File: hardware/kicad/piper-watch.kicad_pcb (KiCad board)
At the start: 2 copper layers, 70 x 50 mm, 15 parts, among them J1 19V in (switched, fused), J3 motor: A1 A2 B1 B2, J4 to ESP32: STEP DIR EN HALL 3V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, J5 to Hall: 5V GND OUT, J6 to buck: 19V, GND, 5V, U1 BTT TMC2209

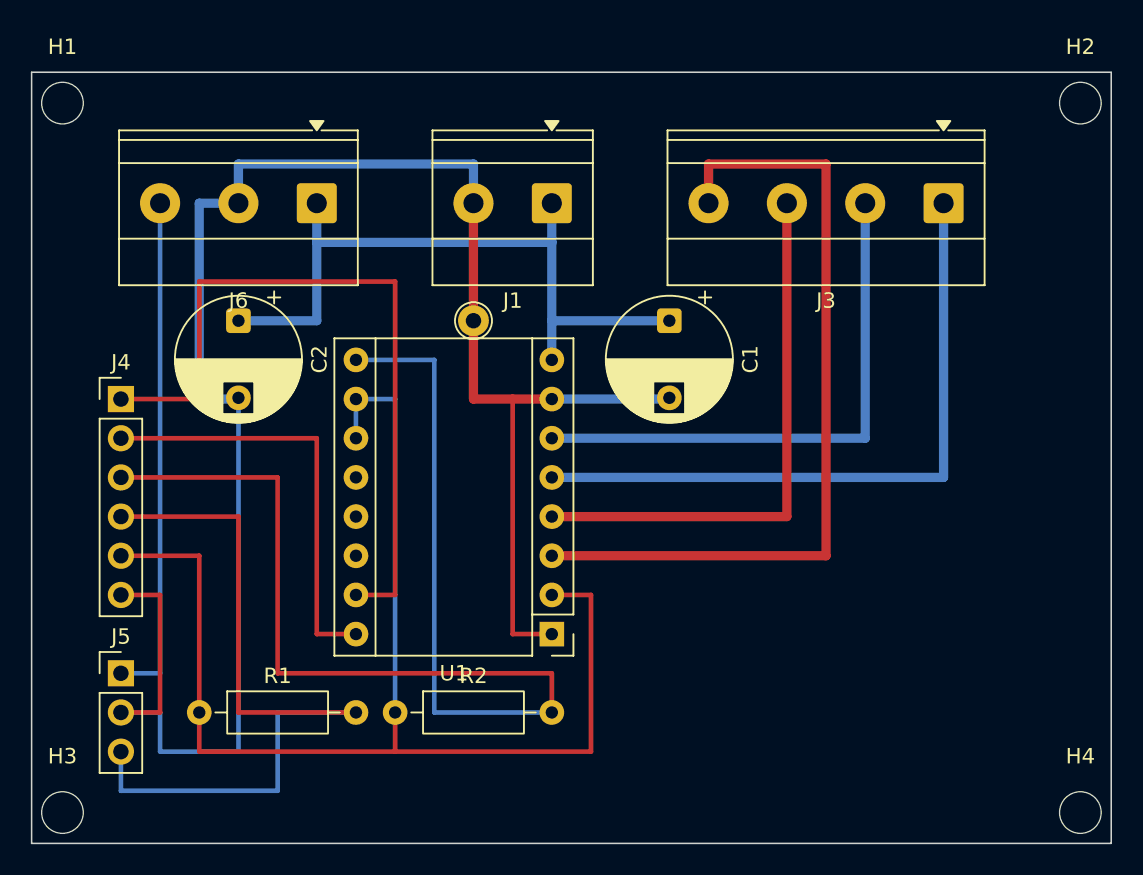
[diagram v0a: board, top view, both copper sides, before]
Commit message: Perfboard: driver turned under J3 (coil wires straight up, A2 A1 B1 B2), J1 + next to J6 19V, C1 above VS; C2 dropped
Co-Authored-By: Claude Opus 5.5 <noreply@anthropic.com>
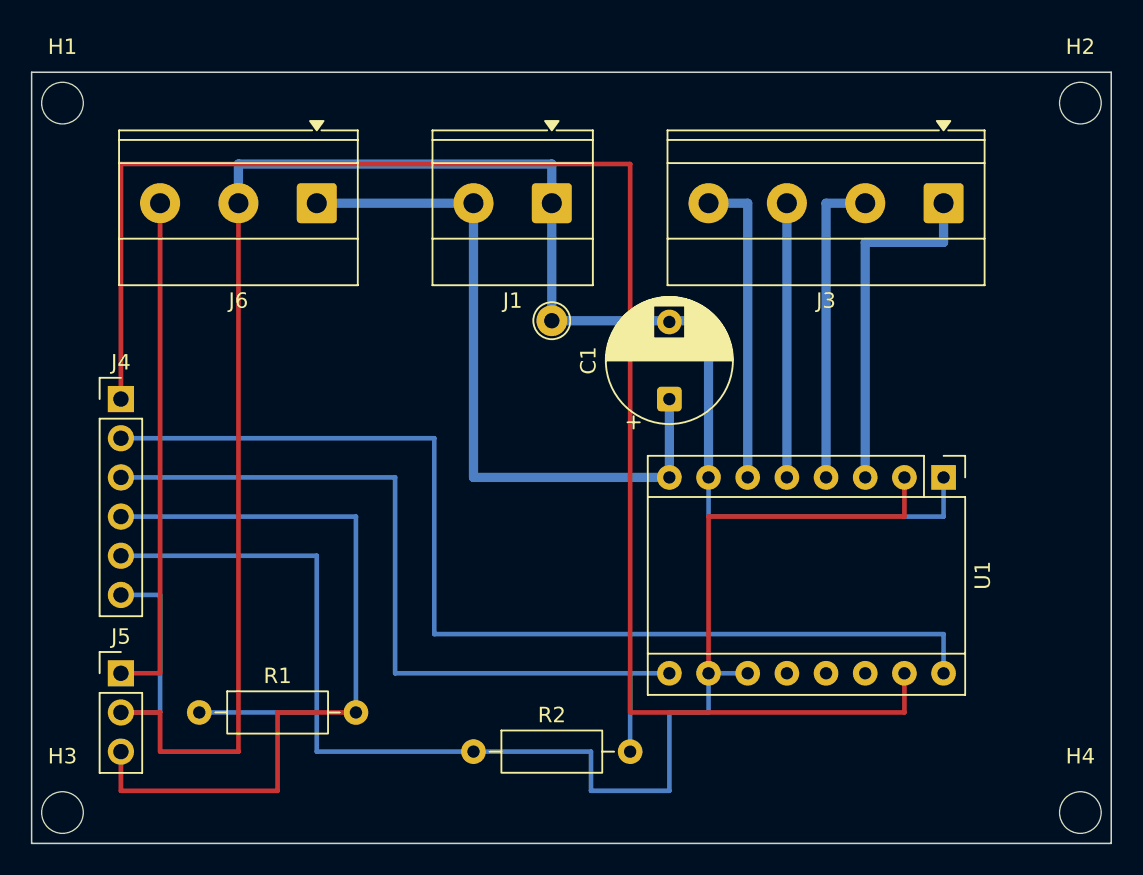
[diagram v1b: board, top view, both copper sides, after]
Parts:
- removed C2: 100uF 50V (opt., at J1), Capacitor_THT:CP_Radial_D8.0mm_P5.00mm
- J1: value 19V in (switched, fused) -> 19V in: + - left to right
- J3: value motor: A1 A2 B1 B2 -> motor: A2 A1 B1 B2 (left to right on the board)
- moved U1 27.4 mm to (159.1, 126.3), turned to -90 degrees
- moved R2 5.68 mm to (128.6, 144.1)
- moved C1 5.08 mm to (141.3, 121.2), turned to 90 degrees
- moved GP1 5.08 mm to (133.7, 116.1)
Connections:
- J1 pad 1: +19V_SW -> GND
- J1 pad 2: GND -> +19V_SW
- J3 pad 1: /Level 2 drive/MOT_A1 -> /Level 2 drive/MOT_B2
- J3 pad 2: /Level 2 drive/MOT_A2 -> /Level 2 drive/MOT_B1
- J3 pad 3: /Level 2 drive/MOT_B1 -> /Level 2 drive/MOT_A1
- J3 pad 4: /Level 2 drive/MOT_B2 -> /Level 2 drive/MOT_A2
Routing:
- net /Level 2 drive/STEP: track 48.3 -> 104.1 mm
- net /Level 2 drive/DIR: track 27.9 -> 68.6 mm
- net /Level 2 drive/MOT_B2: track 53.3 -> 22.9 mm
- net /Level 2 drive/MOT_A1: track 43.2 -> 17.8 mm
- net /Level 2 drive/EN: track 78.7 -> 53.3 mm
- net /Level 2 drive/MOT_B1: track 35.6 -> 20.3 mm
- net /Level 2 drive/MOT_A2: track 35.6 -> 20.3 mm
- net /Level 2 drive/+3V3: track 83.8 -> 96.5 mm
- net GND: track 127.0 -> 132.1 mm

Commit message: Perfboard: J5 under J6, J4 below; wires coloured by net; insulated wires may cross; wiring.md shows the picture
Co-Authored-By: Claude Opus 5.5 <noreply@anthropic.com>
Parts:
- moved J5 22.9 mm to (105.8, 116.1)
- moved J4 5.08 mm to (105.8, 126.3)
- moved R1 2.54 mm to (110.9, 144.1)
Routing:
- net /Level 2 drive/STEP: track 104.1 -> 68.6 mm
- net +5V: track 33.0 -> 10.2 mm
- net /Level 2 drive/+3V3: track 96.5 -> 81.3 mm
- net /Level 2 drive/HALL: track 50.8 -> 43.2 mm
- net GND: track 132.1 -> 127.0 mm
- net /Level 2 drive/DIR: track 68.6 -> 63.5 mm
- net /Level 2 drive/EN: track 53.3 -> 50.8 mm
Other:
- copper layers 2 -> 4

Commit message: Perfboard: jacks one hole closer to the edges; C1 100 uF / 35 V as fitted
Co-Authored-By: Claude Opus 5.5 <noreply@anthropic.com>
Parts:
- C1: value 100uF 50V (at U1 VS) -> 100uF 35V (at U1 VS)
- moved J6 2.54 mm to (118.5, 106.0)
- moved J1 2.54 mm to (133.7, 106.0)
- moved J3 2.54 mm to (159.1, 106.0)
- moved J4 2.54 mm to (103.2, 126.3)
- moved J5 2.54 mm to (103.2, 116.1)
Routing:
- net GND: track 127.0 -> 132.1 mm
- net +5V: track 10.2 -> 15.2 mm
- net +19V_SW: track 45.7 -> 48.3 mm
- net /Level 2 drive/STEP: track 68.6 -> 71.1 mm
- net /Level 2 drive/MOT_B2: track 22.9 -> 25.4 mm
- net /Level 2 drive/MOT_B1: track 20.3 -> 22.9 mm
- net /Level 2 drive/MOT_A1: track 17.8 -> 20.3 mm
- net /Level 2 drive/EN: track 50.8 -> 53.3 mm
- net /Level 2 drive/DIR: track 63.5 -> 66.0 mm
- net /Level 2 drive/MOT_A2: track 20.3 -> 22.9 mm
- net /Level 2 drive/+3V3: track 81.3 -> 83.8 mm
- net /Level 2 drive/HALL: track 43.2 -> 45.7 mm

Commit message: One ESP32: the JC4827W543R display's ESP32-S3 runs the pan motor - J4 lead from its P3 (IO15 STEP, IO16 DIR, IO6 EN, IO7 HALL) and P4 (3.3V, GND); R2 now fitted; base DevKit dropped from wiring.md, schematic, READMEs
Co-Authored-By: Claude Opus 5.5 <noreply@anthropic.com>
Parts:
- J4: value to ESP32: STEP DIR EN HALL 3V3 GND -> to display P3/P4: STEP DIR EN HALL 3V3 GND
- R2: value 10k (opt., EN pull-up) -> 10k (EN pull-up)
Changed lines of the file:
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@@
 			)
 		)
-		(property "Value" "to ESP32: STEP DIR EN HALL 3V3 GND"
+		(property "Value" "to display P3/P4: STEP DIR EN HALL 3V3 GND"
 			(at 0 15.08 0)
 			(layer "F.Fab")
@@
 			)
 		)
-		(property "Value" "10k (opt., EN pull-up)"
+		(property "Value" "10k (EN pull-up)"
 			(at 5.08 2.37 0)
 			(layer "F.Fab")
@@
 	)
 	(segment
-		(start 118.489999 105.95)
-		(end 128.649999 105.95)
-		(width 0.6)
-		(layer "B.Cu")
-		(net "+19V_SW")
-	)
-	(segment
-		(start 128.649999 105.95)
-		(end 128.649999 126.27)
-		(width 0.6)
-		(layer "B.Cu")
-		(net "+19V_SW")
-	)
-	(segment
-		(start 128.649999 126.27)
-		(end 141.35 126.27)
-		(width 0.6)
-		(layer "B.Cu")
-		(net "+19V_SW")
-	)
-	(segment
-		(start 141.35 121.19)
-		(end 141.35 126.27)
-		(width 0.6)
-		(layer "B.Cu")
-		(net "+19V_SW")
-	)
-	(segment
 		(start 159.13 116.11)
 		(end 141.35 116.11)
@@
 	)
 	(segment
-		(start 108.329999 105.95)
-		(end 108.329999 116.11)
-		(width 0.3)
-		(layer "B.Cu")
-		(net "+5V")
-	)
-	(segment
-		(start 108.329999 116.11)
-		(end 103.249999 116.11)
-		(width 0.3)
-		(layer "B.Cu")
-		(net "+5V")
-	)
-	(segment
-		(start 154.049999 126.27)
-		(end 154.049999 108.49)
-		(width 0.6)
-		(layer "B.Cu")
-		(net "/Level 2 drive/MOT_B2")
-	)
-	(segment
-		(start 154.049999 108.49)
-		(end 159.13 108.49)
-		(width 0.6)
-		(layer "B.Cu")
-		(net "/Level 2 drive/MOT_B2")
-	)
-	(segment
-		(start 159.13 108.49)
-		(end 159.13 105.95)
-		(width 0.6)
-		(layer "B.Cu")
-		(net "/Level 2 drive/MOT_B2")
-	)
-	(segment
-		(start 151.51 105.95)
-		(end 154.049999 105.95)
-		(width 0.6)
-		(layer "B.Cu")
-		(net "/Level 2 drive/MOT_B1")
-	)
-	(segment
-		(start 151.51 126.27)
-		(end 151.51 105.95)
-		(width 0.6)
-		(layer "B.Cu")
-		(net "/Level 2 drive/MOT_B1")
-	)
-	(segment
-		(start 148.969999 126.27)
-		(end 148.969999 105.95)
-		(width 0.6)
-		(layer "B.Cu")
-		(net "/Level 2 drive/MOT_A1")
-	)
-	(segment
-		(start 146.429999 105.95)
-		(end 143.89 105.95)
-		(width 0.6)
-		(layer "B.Cu")
-		(net "/Level 2 drive/MOT_A2")
-	)
-	(segment
-		(start 146.429999 126.27)
-		(end 146.429999 105.95)
-		(width 0.6)
-		(layer "B.Cu")
-		(net "/Level 2 drive/MOT_A2")
-	)
-	(segment
-		(start 105.789999 121.19)
-		(end 105.789999 133.889999)
-		(width 0.3)
-		(layer "B.Cu")
-		(net "/Level 2 drive/HALL")
-	)
-	(segment
-		(start 105.789999 133.889999)
-		(end 103.249999 133.889999)
-		(width 0.3)
-		(layer "B.Cu")
-		(net "/Level 2 drive/HALL")
-	)
-	(segment
-		(start 103.249999 121.19)
-		(end 105.789999 121.19)
-		(width 0.3)
-		(layer "B.Cu")
-		(net "/Level 2 drive/HALL")
-	)
-	(segment
-		(start 121.029999 144.05)
-		(end 121.029999 133.889999)
-		(width 0.3)
-		(layer "In1.Cu")
-		(net "/Level 2 drive/HALL")
-	)
-	(segment
-		(start 121.029999 133.889999)
-		(end 103.249999 133.889999)
-		(width 0.3)
-		(layer "In1.Cu")
-		(net "/Level 2 drive/HALL")
-	)
-	(segment
 		(start 103.249999 126.27)
 		(end 126.109999 126.27)
@@
 	)
 	(segment
+		(start 105.789999 121.19)
+		(end 105.789999 133.889999)
+		(width 0.3)
+		(layer "B.Cu")
+		(net "/Level 2 drive/HALL")
+	)
+	(segment
+		(start 105.789999 133.889999)
+		(end 103.249999 133.889999)
+		(width 0.3)
+		(layer "B.Cu")
+		(net "/Level 2 drive/HALL")
+	)
+	(segment
+		(start 103.249999 121.19)
+		(end 105.789999 121.19)
+		(width 0.3)
+		(layer "B.Cu")
+		(net "/Level 2 drive/HALL")
+	)
+	(segment
+		(start 121.029999 144.05)
+		(end 121.029999 133.889999)
+		(width 0.3)
+		(layer "In1.Cu")
+		(net "/Level 2 drive/HALL")
+	)
+	(segment
+		(start 121.029999 133.889999)
+		(end 103.249999 133.889999)
+		(width 0.3)
+		(layer "In1.Cu")
+		(net "/Level 2 drive/HALL")
+	)
+	(segment
 		(start 128.649999 144.05)
 		(end 128.649999 136.43)
@@
 		(net "/Level 2 drive/+3V3")
 	)
+	(segment
+		(start 118.489999 105.95)
+		(end 128.649999 105.95)
+		(width 0.6)
+		(layer "B.Cu")
+		(net "+19V_SW")
+	)
+	(segment
+		(start 128.649999 105.95)
+		(end 128.649999 126.27)
+		(width 0.6)
+		(layer "B.Cu")
+		(net "+19V_SW")
+	)
+	(segment
+		(start 128.649999 126.27)
+		(end 141.35 126.27)
+		(width 0.6)
+		(layer "B.Cu")
+		(net "+19V_SW")
+	)
+	(segment
+		(start 141.35 121.19)
+		(end 141.35 126.27)
+		(width 0.6)
+		(layer "B.Cu")
+		(net "+19V_SW")
+	)
+	(segment
+		(start 154.049999 126.27)
+		(end 154.049999 108.49)
+		(width 0.6)
+		(layer "B.Cu")
+		(net "/Level 2 drive/MOT_B2")
+	)
+	(segment
+		(start 154.049999 108.49)
+		(end 159.13 108.49)
+		(width 0.6)
+		(layer "B.Cu")
+		(net "/Level 2 drive/MOT_B2")
+	)
+	(segment
+		(start 159.13 108.49)
+		(end 159.13 105.95)
+		(width 0.6)
+		(layer "B.Cu")
+		(net "/Level 2 drive/MOT_B2")
+	)
+	(segment
+		(start 151.51 105.95)
+		(end 154.049999 105.95)
+		(width 0.6)
+		(layer "B.Cu")
+		(net "/Level 2 drive/MOT_B1")
+	)
+	(segment
+		(start 151.51 126.27)
+		(end 151.51 105.95)
+		(width 0.6)
+		(layer "B.Cu")
+		(net "/Level 2 drive/MOT_B1")
+	)
+	(segment
+		(start 148.969999 126.27)
+		(end 148.969999 105.95)
+		(width 0.6)
+		(layer "B.Cu")
+		(net "/Level 2 drive/MOT_A1")
+	)
+	(segment
+		(start 146.429999 105.95)
+		(end 143.89 105.95)
+		(width 0.6)
+		(layer "B.Cu")
+		(net "/Level 2 drive/MOT_A2")
+	)
+	(segment
+		(start 146.429999 126.27)
+		(end 146.429999 105.95)
+		(width 0.6)
+		(layer "B.Cu")
+		(net "/Level 2 drive/MOT_A2")
+	)
+	(segment
+		(start 108.329999 105.95)
+		(end 108.329999 116.11)
+		(width 0.3)
+		(layer "B.Cu")
+		(net "+5V")
+	)
+	(segment
+		(start 108.329999 116.11)
+		(end 103.249999 116.11)
+		(width 0.3)
+		(layer "B.Cu")
+		(net "+5V")
+	)
 	(embedded_fonts no)
